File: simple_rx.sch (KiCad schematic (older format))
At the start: 72 parts, among them P1 CONN_01X08, P2 CONN_01X08, P3 CONN_01X03, P4 CONN_01X03, U1 TL072, U2 LM7805CT, U3 LM7905CT, U4 TL072

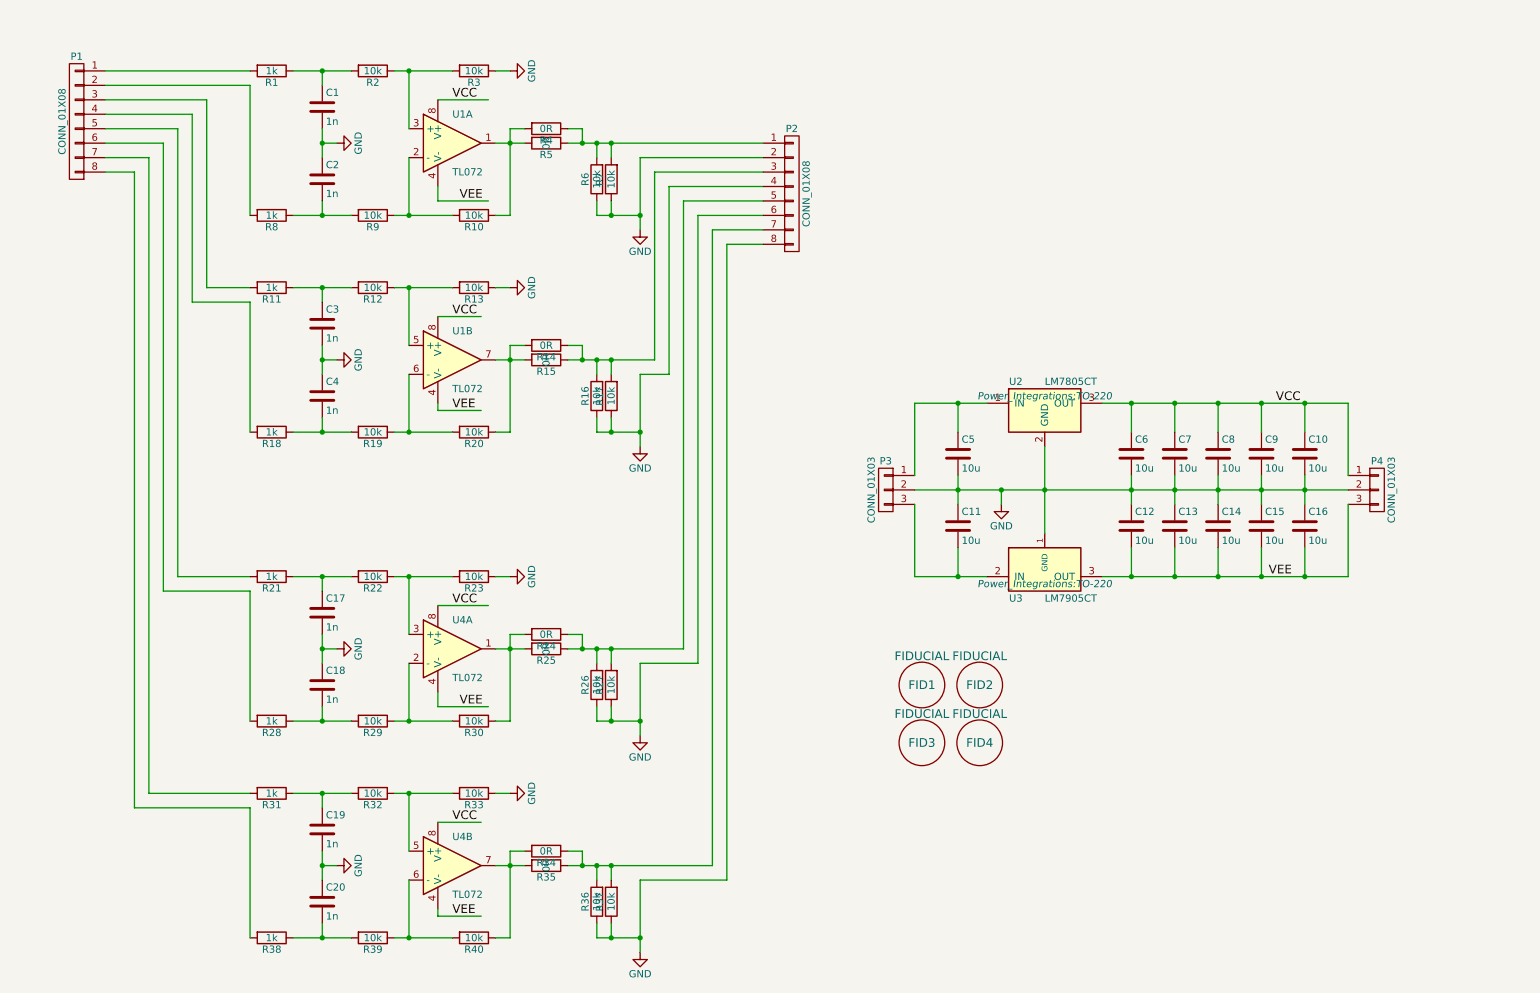
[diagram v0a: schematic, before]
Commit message: converted power regulators to LM317/337 for higher voltage support
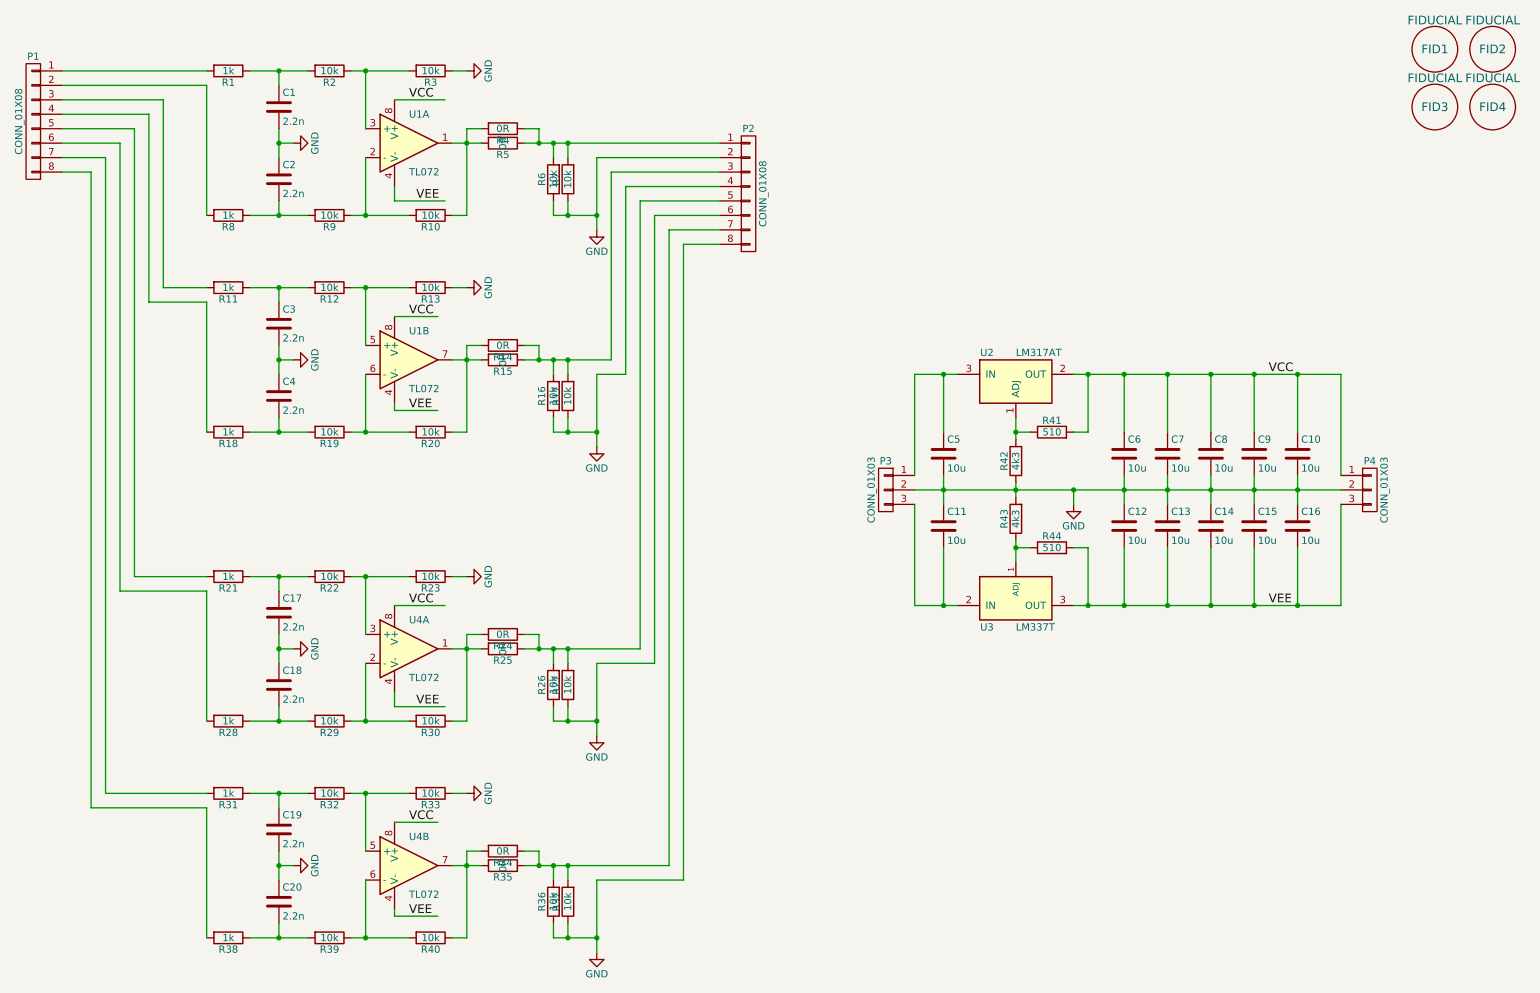
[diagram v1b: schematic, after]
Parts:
- removed U2: LM7805CT, Power_Integrations:TO-220, symbol LM7805CT
- removed U3: LM7905CT, Power_Integrations:TO-220, symbol LM7905CT
- added R41, R44: 510, Resistors_SMD:R_0805, symbol R
- added R42, R43: 4k3, Resistors_SMD:R_0805, symbol R
- added U2: LM317AT, Power_Integrations:TO-220, symbol LM317AT
- added U3: LM337T, Power_Integrations:TO-220, symbol LM337T
- C1, C17, C18, C19, C2, C20, C3, C4: value 1n -> 2.2n
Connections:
- wire segments 177 -> 185
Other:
- moved on the sheet: C1, C10, C11, C12, C13, C14, C15, C16, C17, C18, C19, C2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
